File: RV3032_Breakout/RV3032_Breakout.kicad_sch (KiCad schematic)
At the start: 10 parts, among them J1 Conn_01x04_Female, J2 Conn_01x05_Female

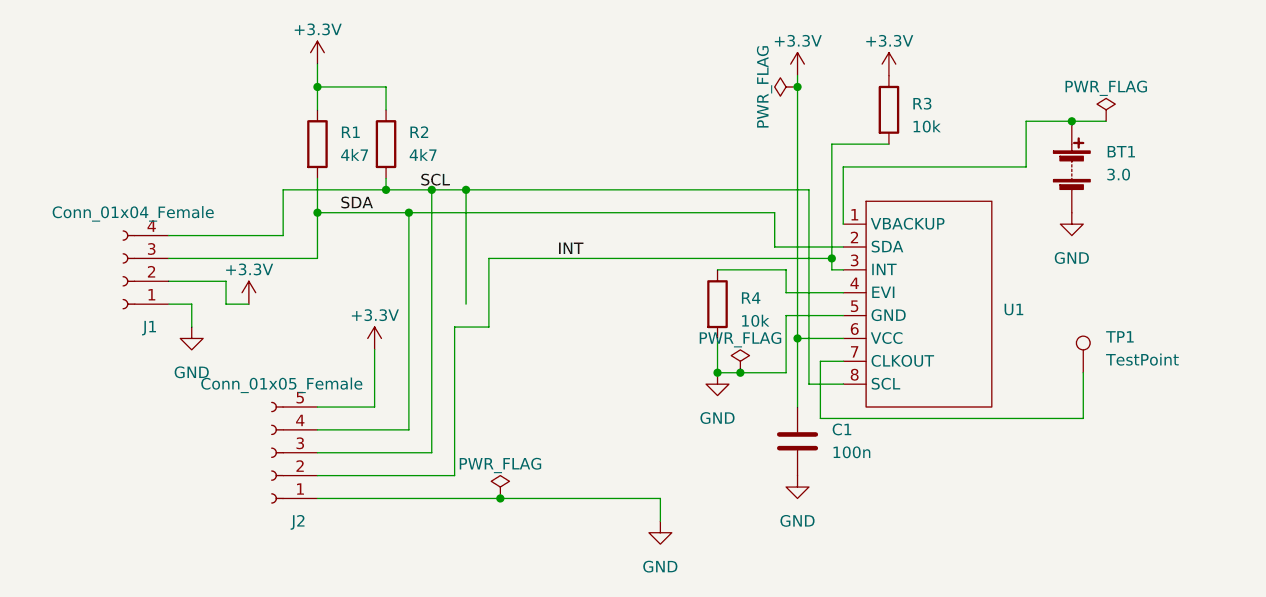
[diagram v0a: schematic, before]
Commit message: Updated to use supercap instead of battery
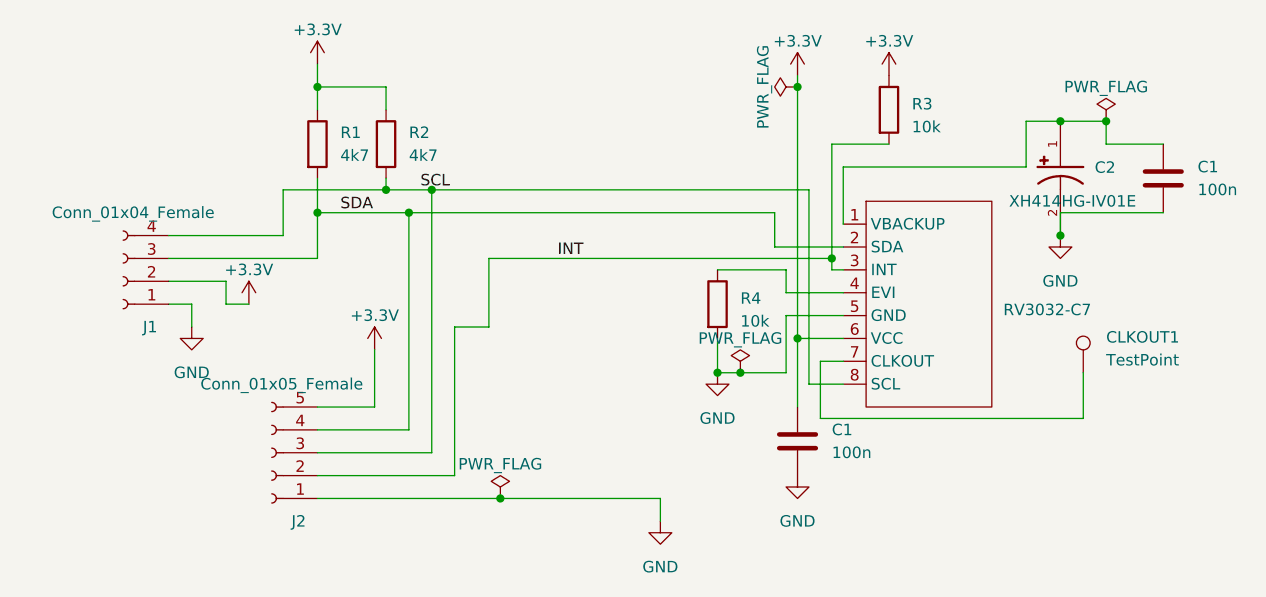
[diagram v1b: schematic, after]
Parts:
- removed BT1: 3.0, Battery:CR44_Tabs, symbol Device:Battery
- added C1: 100n, Capacitor_SMD:C_0603_1608Metric, symbol Device:C
- added C2: XH414HG-IV01E, CAP_XH414HG-IV01E, symbol Larry_Library:XH414HG-IV01E
- renumbered TP1 to CLKOUT1, U1 to RV3032-C7
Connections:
- net GND: now also C1.2, C2.2
- net at RV3032-C7.1 (VBACKUP): now also C1.1, C2.1
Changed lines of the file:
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@@
   (junction (at 118.11 83.82) (diameter 0) (color 0 0 0 0)
   )
-  (junction (at 127 83.82) (diameter 0) (color 0 0 0 0)
-  )
   (junction (at 163.83 72.39) (diameter 0) (color 0 0 0 0)
   )
@@
   (junction (at 154.94 104.14) (diameter 0) (color 0 0 0 0)
   )
+  (junction (at 198.12 76.2) (diameter 0) (color 0 0 0 0)
+  )
   (junction (at 110.49 72.39) (diameter 0) (color 0 0 0 0)
   )
   (junction (at 163.83 100.33) (diameter 0) (color 0 0 0 0)
   )
+  (junction (at 193.04 88.9) (diameter 0) (color 0 0 0 0)
+  )
   (junction (at 167.64 91.44) (diameter 0) (color 0 0 0 0)
   )
-  (junction (at 194.31 76.2) (diameter 0) (color 0 0 0 0)
+  (junction (at 193.04 76.2) (diameter 0) (color 0 0 0 0)
   )
   (junction (at 130.81 118.11) (diameter 0) (color 0 0 0 0)
@@
     (stroke (width 0) (type default))
   )
-  (wire (pts (xy 127 96.52) (xy 127 83.82))
-    (stroke (width 0) (type default))
-  )
   (wire (pts (xy 195.58 109.22) (xy 195.58 104.14))
     (stroke (width 0) (type default))
@@
     (stroke (width 0) (type default))
   )
+  (wire (pts (xy 204.47 86.36) (xy 193.04 86.36))
+    (stroke (width 0) (type default))
+  )
   (wire (pts (xy 93.98 88.9) (xy 106.68 88.9))
     (stroke (width 0) (type default))
@@
     (stroke (width 0) (type default))
   )
-  (wire (pts (xy 194.31 76.2) (xy 198.12 76.2))
-    (stroke (width 0) (type default))
-  )
-  (wire (pts (xy 189.23 76.2) (xy 194.31 76.2))
+  (wire (pts (xy 189.23 76.2) (xy 193.04 76.2))
     (stroke (width 0) (type default))
   )
@@
     (stroke (width 0) (type default))
   )
+  (wire (pts (xy 204.47 78.74) (xy 198.12 78.74))
+    (stroke (width 0) (type default))
+  )
   (wire (pts (xy 110.49 107.95) (xy 116.84 107.95))
     (stroke (width 0) (type default))
@@
     (stroke (width 0) (type default))
   )
-  (wire (pts (xy 127 83.82) (xy 165.1 83.82))
+  (wire (pts (xy 193.04 76.2) (xy 198.12 76.2))
+    (stroke (width 0) (type default))
+  )
+  (wire (pts (xy 198.12 78.74) (xy 198.12 76.2))
+    (stroke (width 0) (type default))
+  )
+  (wire (pts (xy 193.04 86.36) (xy 193.04 88.9))
     (stroke (width 0) (type default))
   )
@@
     (stroke (width 0) (type default))
   )
-  (wire (pts (xy 127 83.82) (xy 123.19 83.82))
+  (wire (pts (xy 123.19 83.82) (xy 165.1 83.82))
     (stroke (width 0) (type default))
   )
@@
       (project "RV3032_Breakout"
         (path "/fcb7a57b-ad59-4476-a702-009410f58d39"
-          (reference "J1") (unit 1)
+          (reference "QWIIC1") (unit 1)
         )
       )
@@
     )
   )
-  (symbol (lib_id "power:GND") (at 194.31 86.36 0) (unit 1)
-    (in_bom yes) (on_board yes) (dnp no) (fields_autoplaced)
-    (property "Reference" "#PWR08" (at 194.31 92.71 0)
-      (effects (font (size 1.27 1.27)) hide)
-    )
-    (property "Value" "GND" (at 194.31 91.44 0)
-      (effects (font (size 1.27 1.27)))
-    )
-    (property "Footprint" "" (at 194.31 86.36 0)
-      (effects (font (size 1.27 1.27)) hide)
-    )
-    (property "Datasheet" "" (at 194.31 86.36 0)
+  (symbol (lib_id "power:GND") (at 193.04 88.9 0) (unit 1)
+    (in_bom yes) (on_board yes) (dnp no) (fields_autoplaced)
+    (property "Reference" "#PWR08" (at 193.04 95.25 0)
+      (effects (font (size 1.27 1.27)) hide)
+    )
+    (property "Value" "GND" (at 193.04 93.98 0)
+      (effects (font (size 1.27 1.27)))
+    )
+    (property "Footprint" "" (at 193.04 88.9 0)
+      (effects (font (size 1.27 1.27)) hide)
+    )
+    (property "Datasheet" "" (at 193.04 88.9 0)
       (effects (font (size 1.27 1.27)) hide)
     )
@@
   (symbol (lib_id "Larry_Library:RV_3032_C7") (at 175.26 93.98 0) (unit 1)
     (in_bom yes) (on_board yes) (dnp no) (fields_autoplaced)
-    (property "Reference" "U1" (at 186.69 97.155 0)
+    (property "Reference" "RV3032-C7" (at 186.69 97.155 0)
       (effects (font (size 1.27 1.27)) (justify left))
     )
@@
       (project "RV3032_Breakout"
         (path "/fcb7a57b-ad59-4476-a702-009410f58d39"
-          (reference "U1") (unit 1)
+          (reference "RV3032-C7") (unit 1)
         )
       )
@@
       (project "RV3032_Breakout"
         (path "/fcb7a57b-ad59-4476-a702-009410f58d39"
-          (reference "J2") (unit 1)
+          (reference "RPI_Header") (unit 1)
+        )
+      )
+    )
+  )
+  (symbol (lib_id "Device:C") (at 204.47 82.55 0) (unit 1)
+    (in_bom yes) (on_board yes) (dnp no) (fields_autoplaced)
+    (property "Reference" "C1" (at 208.28 81.2799 0)
+      (effects (font (size 1.27 1.27)) (justify left))
+    )
+    (property "Value" "100n" (at 208.28 83.8199 0)
+      (effects (font (size 1.27 1.27)) (justify left))
+    )
+    (property "Footprint" "Capacitor_SMD:C_0603_1608Metric" (at 205.4352 86.36 0)
+      (effects (font (size 1.27 1.27)) hide)
+    )
+    (property "Datasheet" "~" (at 204.47 82.55 0)
+      (effects (font (size 1.27 1.27)) hide)
+    )
+    (pin "1")
+    (pin "2")
+    (instances
+      (project "ds3231_plus"
+        (path "/e3aba261-7533-4b3a-9eab-b5cd3c808fd7"
+          (reference "C1") (unit 1)
+        )
+      )
+      (project "RV3032_Breakout"
+        (path "/fcb7a57b-ad59-4476-a702-009410f58d39"
+          (reference "C3") (unit 1)
         )
       )
@@
     )
   )
+  (symbol (lib_id "Larry_Library:XH414HG-IV01E") (at 193.04 81.28 0) (unit 1)
+    (in_bom yes) (on_board yes) (dnp no)
+    (property "Reference" "C2" (at 196.85 81.3401 0)
+      (effects (font (size 1.27 1.27)) (justify left))
+    )
+    (property "Value" "XH414HG-IV01E" (at 187.325 85.09 0)
+      (effects (font (size 1.27 1.27)) (justify left))
+    )
+    (property "Footprint" "CAP_XH414HG-IV01E" (at 193.04 81.28 0)
+      (effects (font (size 1.27 1.27)) (justify bottom) hide)
+    )
+    (property "Datasheet" "" (at 193.04 81.28 0)
+      (effects (font (size 1.27 1.27)) hide)
+    )
+    (property "MANUFACTURER" "Seiko" (at 193.04 81.28 0)
+      (effects (font (size 1.27 1.27)) (justify bottom) hide)
+    )
+    (pin "1")
+    (pin "2")
+    (instances
+      (project "RV3032_Breakout"
+        (path "/fcb7a57b-ad59-4476-a702-009410f58d39"
+          (reference "C2") (unit 1)
+        )
+      )
+    )
+  )
   (symbol (lib_id "power:+3.3V") (at 110.49 69.85 0) (unit 1)
     (in_bom yes) (on_board yes) (dnp no)
@@
     )
   )
-  (symbol (lib_id "Device:Battery") (at 194.31 81.28 0) (unit 1)
-    (in_bom yes) (on_board yes) (dnp no) (fields_autoplaced)
-    (property "Reference" "BT1" (at 198.12 79.6289 0)
-      (effects (font (size 1.27 1.27)) (justify left))
-    )
-    (property "Value" "3.0" (at 198.12 82.1689 0)
-      (effects (font (size 1.27 1.27)) (justify left))
-    )
-    (property "Footprint" "Battery:CR44_Tabs" (at 194.31 79.756 90)
-      (effects (font (size 1.27 1.27)) hide)
-    )
-    (property "Datasheet" "~" (at 194.31 79.756 90)
+  (symbol (lib_id "Device:R") (at 118.11 78.74 0) (unit 1)
+    (in_bom yes) (on_board yes) (dnp no) (fields_autoplaced)
+    (property "Reference" "R2" (at 120.65 77.4699 0)
+      (effects (font (size 1.27 1.27)) (justify left))
+    )
+    (property "Value" "4k7" (at 120.65 80.0099 0)
+      (effects (font (size 1.27 1.27)) (justify left))
+    )
+    (property "Footprint" "Resistor_SMD:R_0603_1608Metric" (at 116.332 78.74 90)
+      (effects (font (size 1.27 1.27)) hide)
+    )
+    (property "Datasheet" "~" (at 118.11 78.74 0)
       (effects (font (size 1.27 1.27)) hide)
     )
@@
       (project "ds3231_plus"
         (path "/e3aba261-7533-4b3a-9eab-b5cd3c808fd7"
-          (reference "BT1") (unit 1)
-        )
-      )
-      (project "RV3032_Breakout"
-        (path "/fcb7a57b-ad59-4476-a702-009410f58d39"
-          (reference "BT1") (unit 1)
-        )
-      )
-    )
-  )
-  (symbol (lib_id "Device:R") (at 118.11 78.74 0) (unit 1)
-    (in_bom yes) (on_board yes) (dnp no) (fields_autoplaced)
-    (property "Reference" "R2" (at 120.65 77.4699 0)
-      (effects (font (size 1.27 1.27)) (justify left))
-    )
-    (property "Value" "4k7" (at 120.65 80.0099 0)
-      (effects (font (size 1.27 1.27)) (justify left))
-    )
-    (property "Footprint" "Resistor_SMD:R_0603_1608Metric" (at 116.332 78.74 90)
-      (effects (font (size 1.27 1.27)) hide)
-    )
-    (property "Datasheet" "~" (at 118.11 78.74 0)
-      (effects (font (size 1.27 1.27)) hide)
-    )
-    (pin "1")
-    (pin "2")
-    (instances
-      (project "ds3231_plus"
-        (path "/e3aba261-7533-4b3a-9eab-b5cd3c808fd7"
           (reference "R2") (unit 1)
         )
@@
   (symbol (lib_id "Connector:TestPoint") (at 195.58 104.14 0) (unit 1)
     (in_bom yes) (on_board yes) (dnp no) (fields_autoplaced)
-    (property "Reference" "TP1" (at 198.12 100.203 0)
+    (property "Reference" "CLKOUT1" (at 198.12 100.203 0)
       (effects (font (size 1.27 1.27)) (justify left))
     )
@@
       (project "RV3032_Breakout"
         (path "/fcb7a57b-ad59-4476-a702-009410f58d39"
-          (reference "TP1") (unit 1)
-        )
-      )
+          (reference "CLKOUT1") (unit 1)
+        )
+      )
